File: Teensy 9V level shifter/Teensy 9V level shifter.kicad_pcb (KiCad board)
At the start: 2 copper layers, 76.5 x 51.2 mm, 47 parts, among them J1 PSU, J10 VGG, J2 TeensyL, J3 CLK, J4 ¬CLK, J5 TeensyR, J6 TeensyL1, J7 TeensyR1, J8 PSU, J9 VCA_CV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

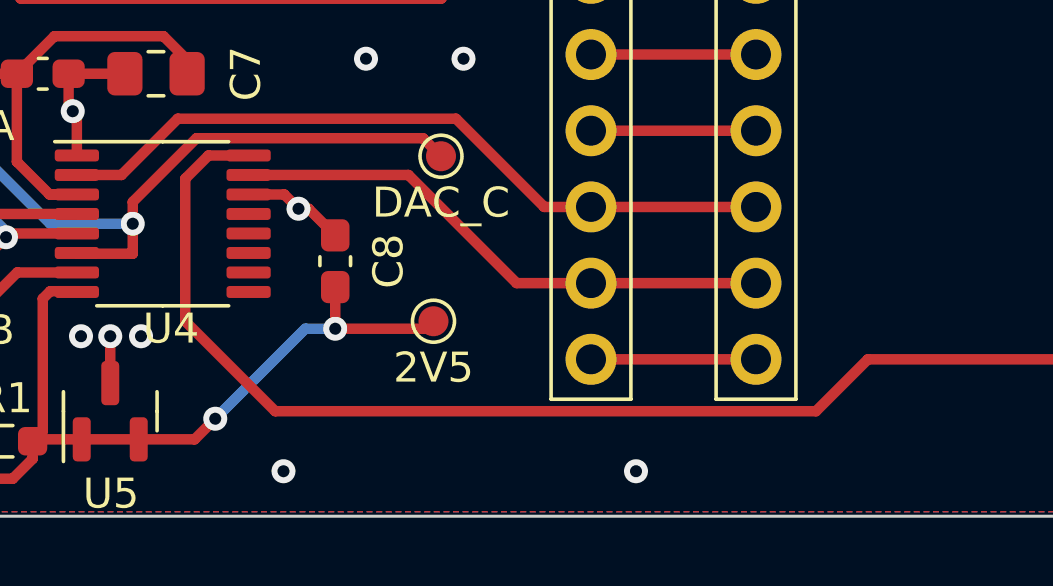
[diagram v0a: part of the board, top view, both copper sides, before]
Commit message: String Maschine controller - fix broken symbols
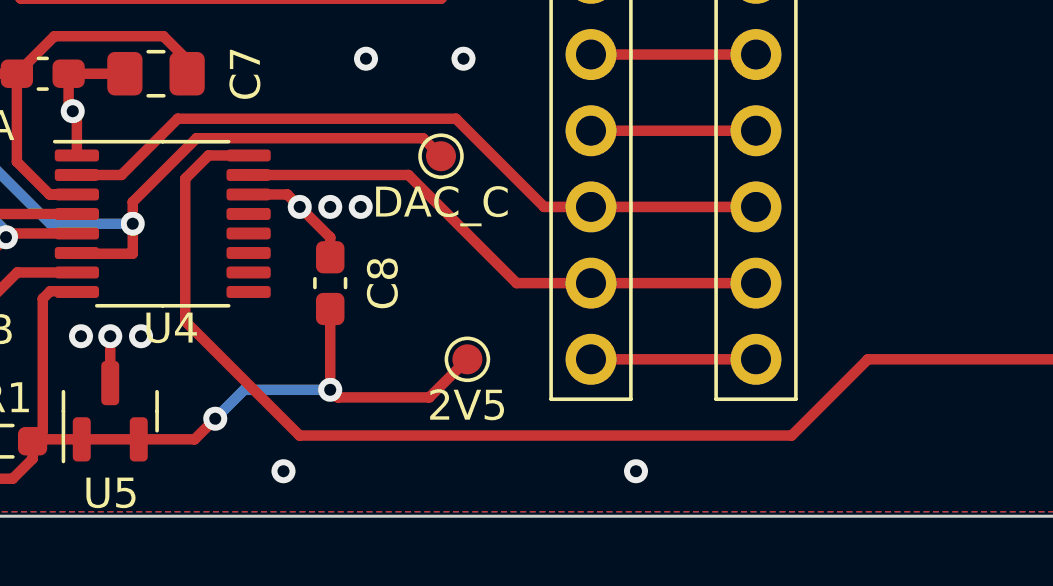
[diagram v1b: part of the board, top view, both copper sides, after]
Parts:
- moved TP1 1.70 mm to (55.9, 96.5)
- moved C8 0.75 mm to (51.3, 94.0)
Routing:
- net 2V5: track 32.3 -> 34.4 mm
- net SCK: track 46.2 -> 46.8 mm
- net GND: track 31.5 -> 32.0 mm, vias 27 -> 29

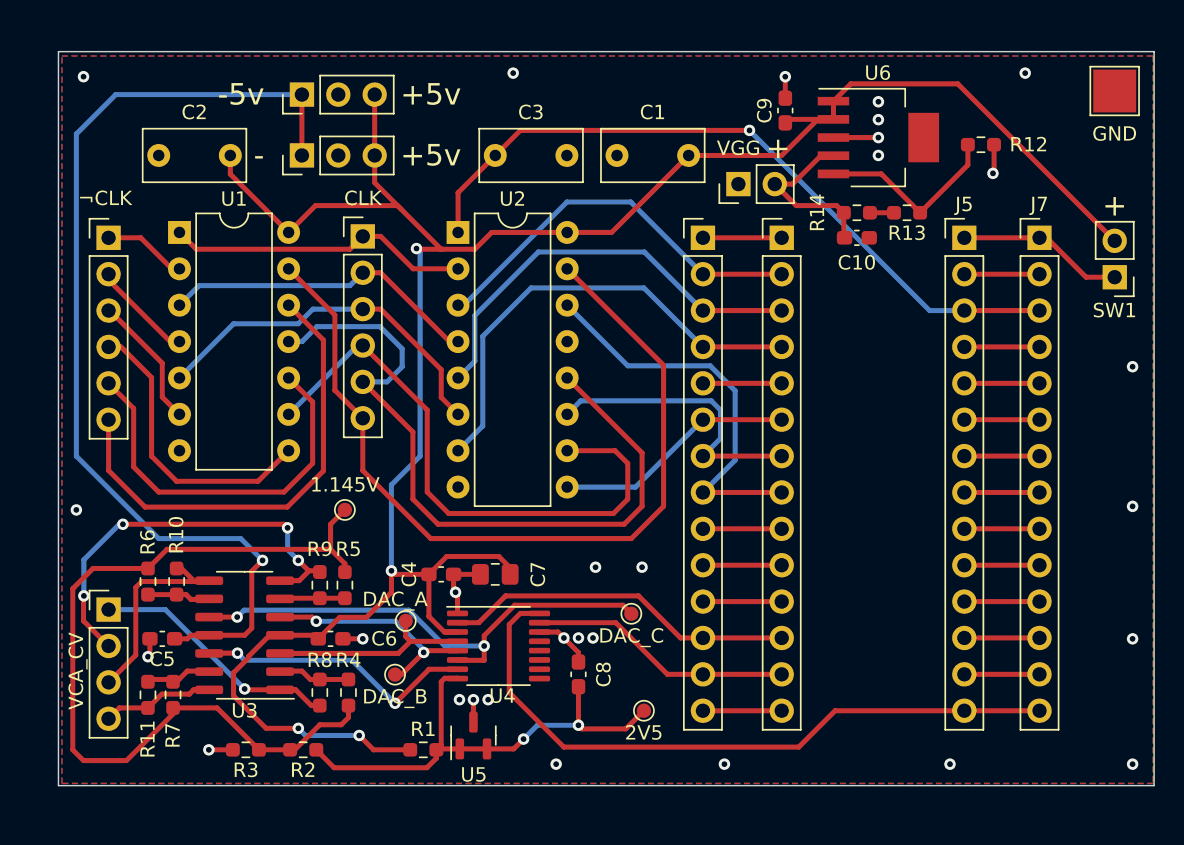
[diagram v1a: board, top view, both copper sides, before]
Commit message: String Maschine - Add simulations and add VCA for controlling the feedback loop
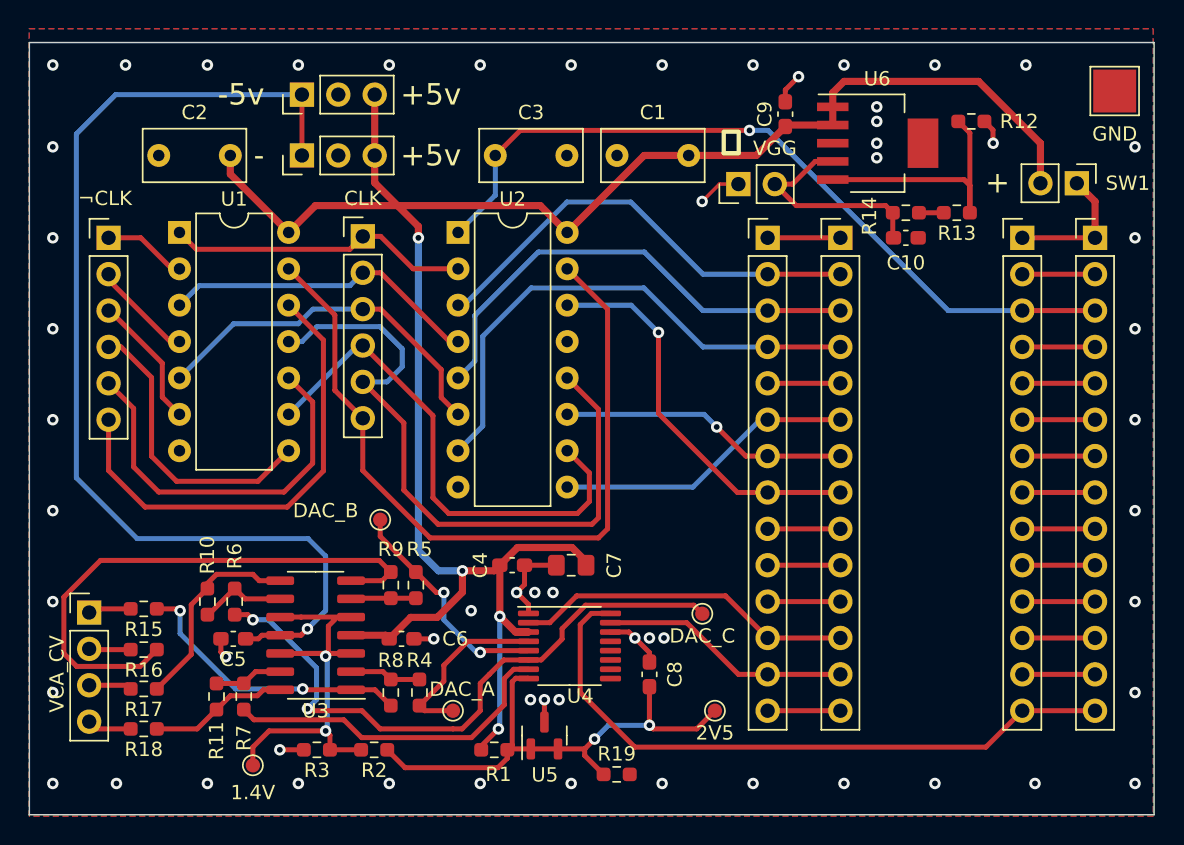
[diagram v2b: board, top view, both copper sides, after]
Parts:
- added R15: 1k, Resistor_SMD:R_0603_1608Metric_Pad0.98x0.95mm_HandSolder, F.Cu at (21.0, 89.4)
- added R16: 1k, Resistor_SMD:R_0603_1608Metric_Pad0.98x0.95mm_HandSolder, F.Cu at (21.0, 92.3)
- added R17: 1k, Resistor_SMD:R_0603_1608Metric_Pad0.98x0.95mm_HandSolder, F.Cu at (21.0, 95.0)
- added R18: 1k, Resistor_SMD:R_0603_1608Metric_Pad0.98x0.95mm_HandSolder, F.Cu at (21.0, 97.8)
- added R19: 1k, Resistor_SMD:R_0603_1608Metric_Pad0.98x0.95mm_HandSolder, F.Cu at (54.0, 101.0)
- R10, R11, R8, R9: value 5.6k -> 20k
- R2: value 5.6k -> 12k
- R3: value 4.7k -> 15k
- TP6: value 1.145V -> 1.4V
- U6: value MCP1826-ADJE/AT -> MCP1826-ADJ
- moved TP6 19.0 mm to (28.6, 100.3), turned to 180 degrees
- moved TP5 10.9 mm to (37.5, 83.2)
- moved TP2 7.08 mm to (42.5, 96.5)
- moved SW1 7.07 mm to (86.1, 59.7), turned to -90 degrees
- moved R6 6.21 mm to (27.3, 88.9), turned to 90 degrees
- moved C7 5.34 mm to (50.8, 86.4)
- moved C4 5.00 mm to (46.7, 86.4)
- moved C6 4.96 mm to (39.0, 91.5)
- moved C8 4.96 mm to (56.3, 94.0)
- moved R2 4.96 mm to (37.0, 99.2)
- moved R3 4.96 mm to (33.0, 99.2)
- moved R4 4.96 mm to (40.2, 95.2)
- moved R5 4.96 mm to (40.0, 87.8)
- moved R8 4.96 mm to (38.2, 95.2)
- moved R9 4.96 mm to (38.2, 87.8)
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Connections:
- R10 pad 2: Net-(J9-Pad3) -> Net-(R10-Pad2)
- R11 pad 2: Net-(J9-Pad4) -> Net-(U3-Pad14)
- R2 pad 2: 1.145V -> 1.4V
- R3 pad 1: 1.145V -> 1.4V
- R4 pad 1: 1.145V -> Net-(R4-Pad1)
- R5 pad 1: 1.145V -> Net-(R5-Pad1)
- R6 pad 1: 1.145V -> Net-(TP4-Pad1)
- R7 pad 1: 1.145V -> Net-(R7-Pad1)
- R8 pad 2: Net-(J9-Pad1) -> Net-(R8-Pad2)
- R9 pad 2: Net-(J9-Pad2) -> Net-(U3-Pad7)
- TP2 pad 1: Net-(U3-Pad3) -> Net-(R4-Pad1)
- TP4 pad 1: Net-(U3-Pad10) -> Net-(TP4-Pad1)
- TP5 pad 1: Net-(U3-Pad5) -> Net-(R5-Pad1)
- TP6 pad 1: 1.145V -> 1.4V
- U3 pad 1: Net-(J9-Pad1) -> Net-(R8-Pad2)
- U3 pad 10: Net-(U3-Pad10) -> 1.4V
- U3 pad 12: Net-(U3-Pad12) -> 1.4V
- U3 pad 14: Net-(J9-Pad4) -> Net-(U3-Pad14)
- U3 pad 3: Net-(U3-Pad3) -> 1.4V
- U3 pad 5: Net-(U3-Pad5) -> 1.4V
- U3 pad 7: Net-(J9-Pad2) -> Net-(U3-Pad7)
- U3 pad 8: Net-(J9-Pad3) -> Net-(R10-Pad2)
- U4 pad 4: Net-(U3-Pad3) -> Net-(R4-Pad1)
- U4 pad 5: Net-(U3-Pad5) -> Net-(R5-Pad1)
- U4 pad 6: Net-(U3-Pad10) -> Net-(TP4-Pad1)
- U4 pad 7: Net-(U3-Pad12) -> Net-(R7-Pad1)
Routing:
- net 1.145V: track 59.9 -> 0.00 mm
- net Net-(TP4-Pad1): track 0.00 -> 43.9 mm, vias 0 -> 2
- net Net-(U3-Pad7): track 0.00 -> 38.5 mm
- net Net-(U3-Pad10): track 35.4 -> 0.00 mm, vias 2 -> 0
- net 1.4V: track 0.00 -> 30.4 mm, vias 0 -> 2
- net Net-(J9-Pad2): track 28.9 -> 2.92 mm, vias 4 -> 0
- net Net-(R7-Pad1): track 0.00 -> 23.7 mm
- net Net-(R8-Pad2): track 0.00 -> 20.1 mm, vias 0 -> 2
- net Net-(U3-Pad12): track 19.8 -> 0.00 mm, vias 2 -> 0
- net Net-(R5-Pad1): track 0.00 -> 16.0 mm, vias 0 -> 2
- net Net-(U3-Pad5): track 16.0 -> 0.00 mm, vias 2 -> 0
- net +5V: track 160.4 -> 145.3 mm
- net Net-(J9-Pad1): track 17.5 -> 3.00 mm, vias 1 -> 0
- net Net-(R10-Pad2): track 0.00 -> 14.4 mm
- net Net-(U3-Pad3): track 14.3 -> 0.00 mm
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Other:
- board size 76.5 x 51.2 mm -> 78.5 x 53.9 mm
- board text added: "⏚"
